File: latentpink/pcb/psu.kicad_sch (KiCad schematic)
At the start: 110 parts, among them J13 CONN_01X05, J14 CONN_01X03, J6 BARREL_JACK, U10 MYMGK1R812ERSR, U11 MYMGK00504ERSR, U12 STM32L031-QFN32, U13 MYMGK00504ERSR, U14 MYMGK00504ERSR, U15 MYMGK00504ERSR, U16 NCP45521IMNTWG-H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

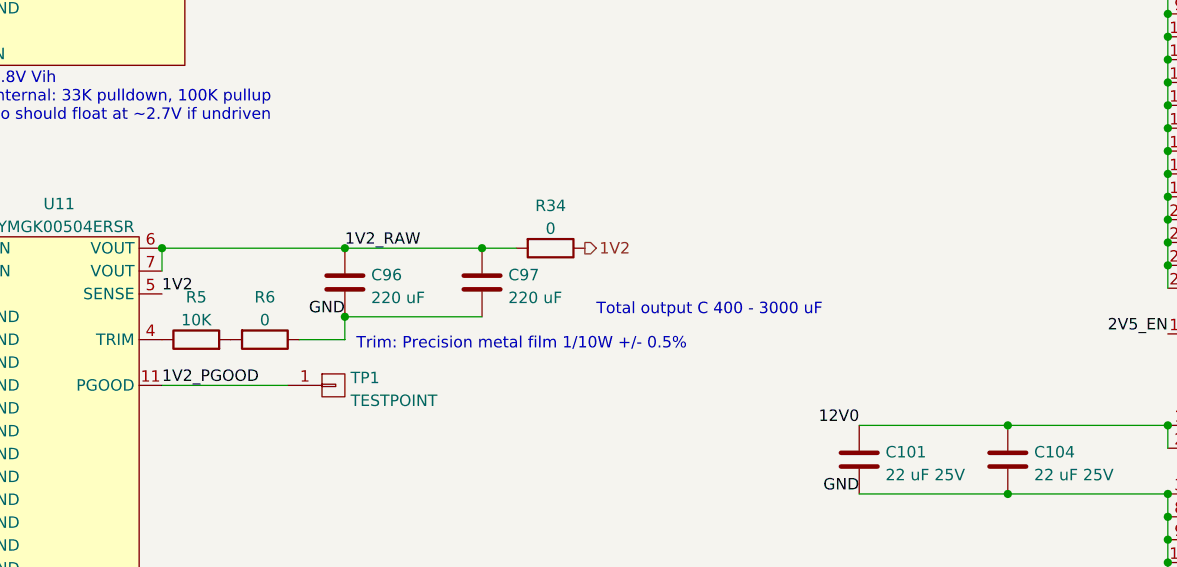
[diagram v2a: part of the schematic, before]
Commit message: Continued work on signoff review, added some more test points and SFP+ activity LEDs
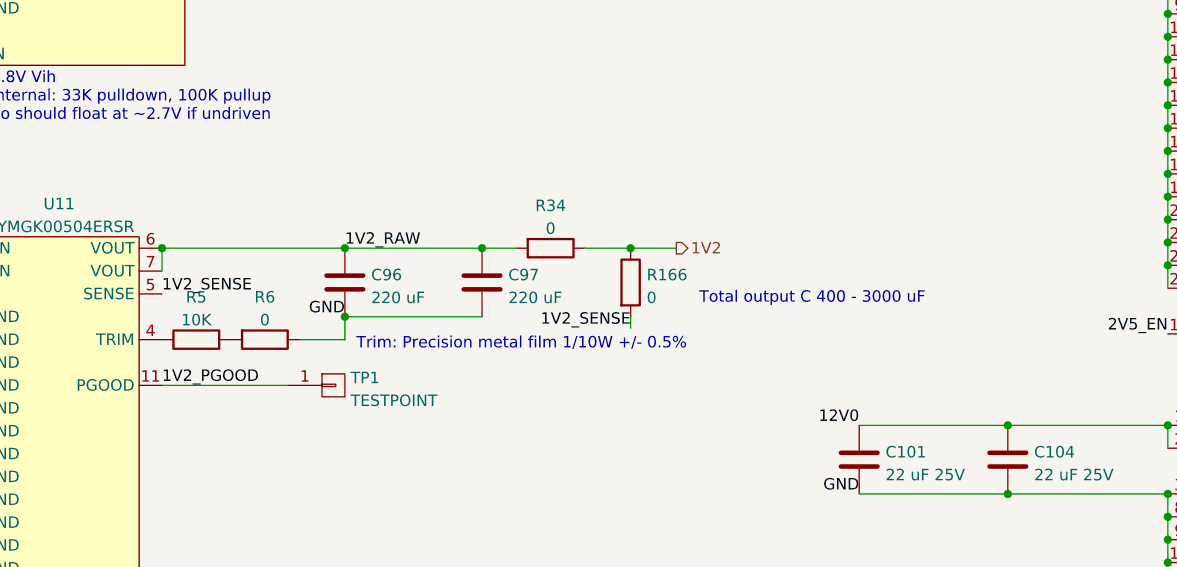
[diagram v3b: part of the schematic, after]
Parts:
- added R166: 0, azonenberg_pcb:EIA_0402_RES_NOSILK, symbol device:R
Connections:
- net 1V2: now also R166.1; no longer U11.5 (SENSE)
- new net 1V2_SENSE: R166.2, U11.5 (SENSE)
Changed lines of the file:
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@@
   (paper "A3")
   (title_block
-    (date "2023-05-20")
+    (date "2023-05-21")
     (rev "0.1")
     (company "Antikernel Labs")
@@
   (junction (at 260.35 102.235) (diameter 0) (color 0 0 0 0)
   )
+  (junction (at 129.54 140.97) (diameter 0) (color 0 0 0 0)
+  )
   (junction (at 374.65 246.38) (diameter 0) (color 0 0 0 0)
   )
@@
     (stroke (width 0) (type default) (color 0 0 0 0))
   )
+  (wire (pts (xy 129.54 148.59) (xy 129.54 149.86))
+    (stroke (width 0) (type default) (color 0 0 0 0))
+  )
   (wire (pts (xy 361.95 246.38) (xy 374.65 246.38))
     (stroke (width 0) (type default) (color 0 0 0 0))
@@
     (stroke (width 0) (type default) (color 0 0 0 0))
   )
+  (wire (pts (xy 129.54 140.97) (xy 134.62 140.97))
+    (stroke (width 0) (type default) (color 0 0 0 0))
+  )
   (wire (pts (xy 54.61 50.8) (xy 54.61 53.34))
     (stroke (width 0) (type default) (color 0 0 0 0))
@@
     (stroke (width 0) (type default) (color 0 0 0 0))
   )
+  (wire (pts (xy 124.46 140.97) (xy 129.54 140.97))
+    (stroke (width 0) (type default) (color 0 0 0 0))
+  )
   (wire (pts (xy 155.575 44.45) (xy 172.085 44.45))
     (stroke (width 0) (type default) (color 0 0 0 0))
@@
     (stroke (width 0) (type default) (color 0 0 0 0))
   )
-  (text "Total output C 400 - 3000 uF" (at 125.73 148.59 0)
+  (text "Total output C 400 - 3000 uF" (at 137.16 147.32 0)
     (effects (font (size 1.27 1.27)) (justify left bottom))
   )
@@
     (effects (font (size 1.27 1.27)) (justify right bottom))
   )
+  (label "1V2_SENSE" (at 129.54 149.86 180)
+    (effects (font (size 1.27 1.27)) (justify right bottom))
+  )
   (label "SUPER_RST_N" (at 255.27 261.62 180)
     (effects (font (size 1.27 1.27)) (justify right bottom))
@@
     (effects (font (size 1.27 1.27)) (justify right bottom))
   )
-  (label "1V2" (at 77.47 146.05 0)
+  (label "1V2_SENSE" (at 77.47 146.05 0)
     (effects (font (size 1.27 1.27)) (justify left bottom))
   )
@@
     (effects (font (size 1.27 1.27)) (justify left))
   )
-  (hierarchical_label "1V2" (shape output) (at 124.46 140.97 0)
+  (hierarchical_label "1V2" (shape output) (at 134.62 140.97 0)
     (effects (font (size 1.27 1.27)) (justify left))
   )
@@
       (effects (font (size 1.27 1.27)) hide)
     )
+    (pin "1")
+    (pin "2")
+  )
+  (symbol (lib_id "device:R") (at 129.54 144.78 0) (unit 1)
+    (in_bom yes) (on_board yes) (fields_autoplaced)
+    (property "Reference" "R166" (id 0) (at 131.318 143.9453 0)
+      (effects (font (size 1.27 1.27)) (justify left))
+    )
+    (property "Value" "0" (id 1) (at 131.318 146.4822 0)
+      (effects (font (size 1.27 1.27)) (justify left))
+    )
+    (property "Footprint" "azonenberg_pcb:EIA_0402_RES_NOSILK" (id 2) (at 127.762 144.78 90)
+      (effects (font (size 1.27 1.27)) hide)
+    )
+    (property "Datasheet" "" (id 3) (at 129.54 144.78 0)
+      (effects (font (size 1.27 1.27)) hide)
+    )

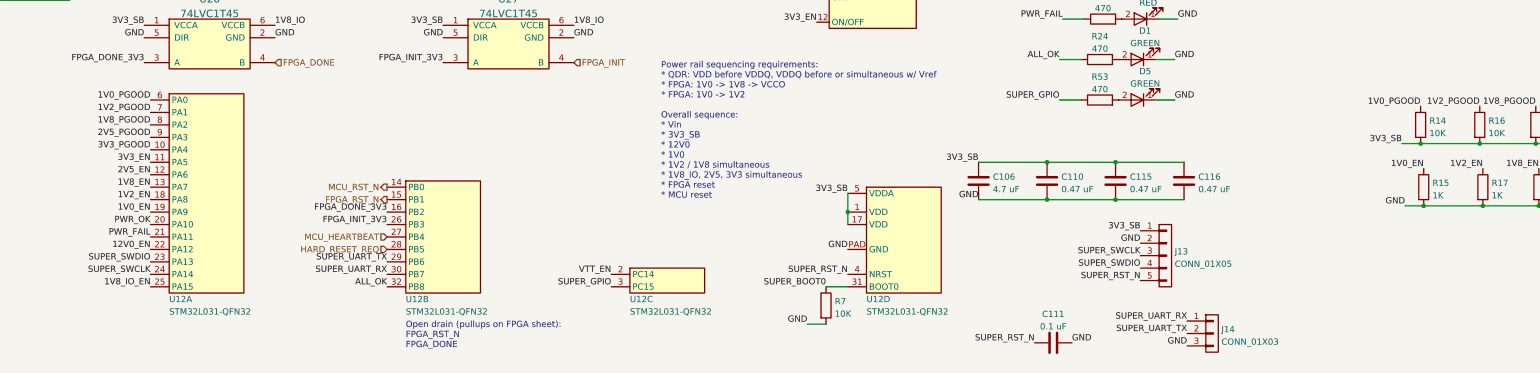
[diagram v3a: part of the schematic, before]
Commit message: Finished initial schematic review, added ESD diodes to Ethernet pairs
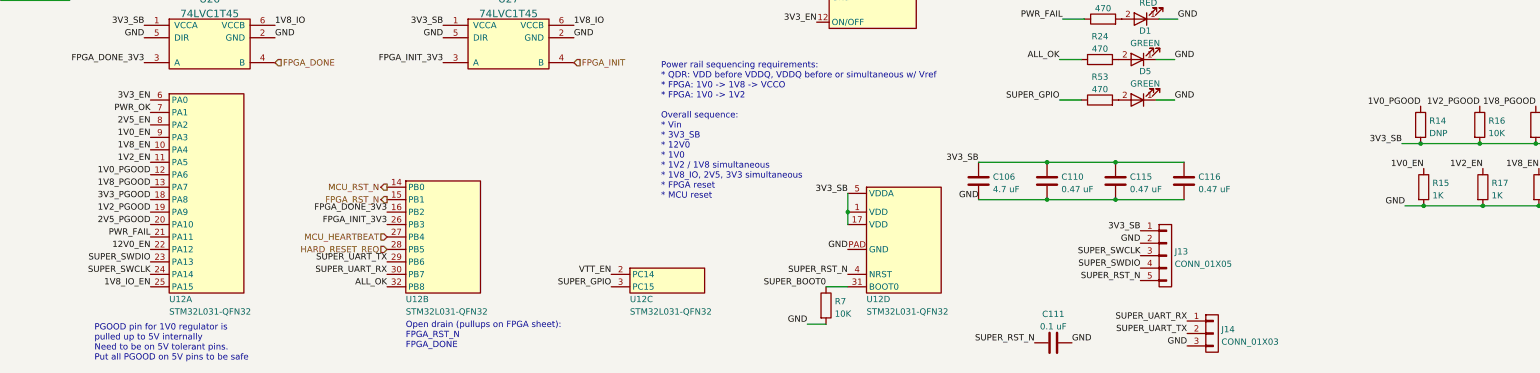
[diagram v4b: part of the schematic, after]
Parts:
- R14: value 10K -> DNP
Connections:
- net 1V0_EN: now also U12.9 (PA3); no longer U12.19 (PA9)
- net 1V0_PGOOD: now also U12.12 (PA6); no longer U12.6 (PA0)
- net 1V2_EN: now also U12.11 (PA5); no longer U12.18 (PA8)
- net 1V2_PGOOD: now also U12.19 (PA9); no longer U12.7 (PA1)
- net 1V8_EN: now also U12.10 (PA4); no longer U12.13 (PA7)
- net 1V8_PGOOD: now also U12.13 (PA7); no longer U12.8 (PA2)
- net 2V5_EN: now also U12.8 (PA2); no longer U12.12 (PA6)
- net 2V5_PGOOD: now also U12.20 (PA10); no longer U12.9 (PA3)
- net 3V3_EN: now also U12.6 (PA0); no longer U12.11 (PA5)
- net 3V3_PGOOD: now also U12.18 (PA8); no longer U12.10 (PA4)
- net PWR_OK: now also U12.7 (PA1); no longer U12.20 (PA10)
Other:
- note added: "PGOOD pin for 1V0 regulator is pulled up to 5V internally Need to be on 5V tolerant pins. Put all PGOOD on 5V pins to be safe"
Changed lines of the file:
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@@
+    (effects (font (size 1.27 1.27)) (justify left bottom))
+  )
+  (text "PGOOD pin for 1V0 regulator is\npulled up to 5V internally\nNeed to be on 5V tolerant pins.\nPut all PGOOD on 5V pins to be safe"
+    (at 41.91 278.13 0)
     (effects (font (size 1.27 1.27)) (justify left bottom))
   )
@@
     (effects (font (size 1.27 1.27)) (justify left bottom))
   )
-  (label "1V2_EN" (at 53.34 245.11 180)
+  (label "1V2_EN" (at 53.34 237.49 180)
     (effects (font (size 1.27 1.27)) (justify right bottom))
   )
@@
     (effects (font (size 1.27 1.27)) (justify left bottom))
   )
-  (label "3V3_PGOOD" (at 53.34 234.95 180)
+  (label "3V3_PGOOD" (at 53.34 245.11 180)
     (effects (font (size 1.27 1.27)) (justify right bottom))
   )
@@
     (effects (font (size 1.27 1.27)) (justify left bottom))
   )
-  (label "1V8_PGOOD" (at 53.34 229.87 180)
+  (label "1V8_PGOOD" (at 53.34 242.57 180)
     (effects (font (size 1.27 1.27)) (justify right bottom))
   )
@@
     (effects (font (size 1.27 1.27)) (justify right bottom))
   )
-  (label "2V5_PGOOD" (at 53.34 232.41 180)
+  (label "2V5_PGOOD" (at 53.34 250.19 180)
     (effects (font (size 1.27 1.27)) (justify right bottom))
   )
@@
     (effects (font (size 1.27 1.27)) (justify right bottom))
   )
-  (label "1V0_PGOOD" (at 53.34 224.79 180)
+  (label "1V0_PGOOD" (at 53.34 240.03 180)
     (effects (font (size 1.27 1.27)) (justify right bottom))
   )
@@
     (effects (font (size 1.27 1.27)) (justify left bottom))
   )
-  (label "1V0_EN" (at 53.34 247.65 180)
+  (label "1V0_EN" (at 53.34 232.41 180)
     (effects (font (size 1.27 1.27)) (justify right bottom))
   )
@@
     (effects (font (size 1.27 1.27)) (justify right bottom))
   )
-  (label "1V2_PGOOD" (at 53.34 227.33 180)
+  (label "1V2_PGOOD" (at 53.34 247.65 180)
     (effects (font (size 1.27 1.27)) (justify right bottom))
   )
@@
     (effects (font (size 1.27 1.27)) (justify right bottom))
   )
-  (label "PWR_OK" (at 53.34 250.19 180)
+  (label "PWR_OK" (at 53.34 227.33 180)
     (effects (font (size 1.27 1.27)) (justify right bottom))
   )
@@
     (effects (font (size 1.27 1.27)) (justify right bottom))
   )
-  (label "2V5_EN" (at 53.34 240.03 180)
+  (label "2V5_EN" (at 53.34 229.87 180)
     (effects (font (size 1.27 1.27)) (justify right bottom))
   )
@@
     (effects (font (size 1.27 1.27)) (justify right bottom))
   )
-  (label "1V8_EN" (at 53.34 242.57 180)
+  (label "1V8_EN" (at 53.34 234.95 180)
     (effects (font (size 1.27 1.27)) (justify right bottom))
   )
@@
     (effects (font (size 1.27 1.27)) (justify right bottom))
   )
-  (label "3V3_EN" (at 53.34 237.49 180)
+  (label "3V3_EN" (at 53.34 224.79 180)
     (effects (font (size 1.27 1.27)) (justify right bottom))
   )
@@
       (effects (font (size 1.27 1.27)) (justify left))
     )
-    (property "Value" "10K" (id 1) (at 314.198 231.5722 0)
-      (effects (font (size 1.27 1.27)) (justify left))
-    )
+    (property "Value" "DNP" (id 1) (at 314.198 231.5722 0)
+      (effects (font (size 1.27 1.27)) (justify left))
+    )

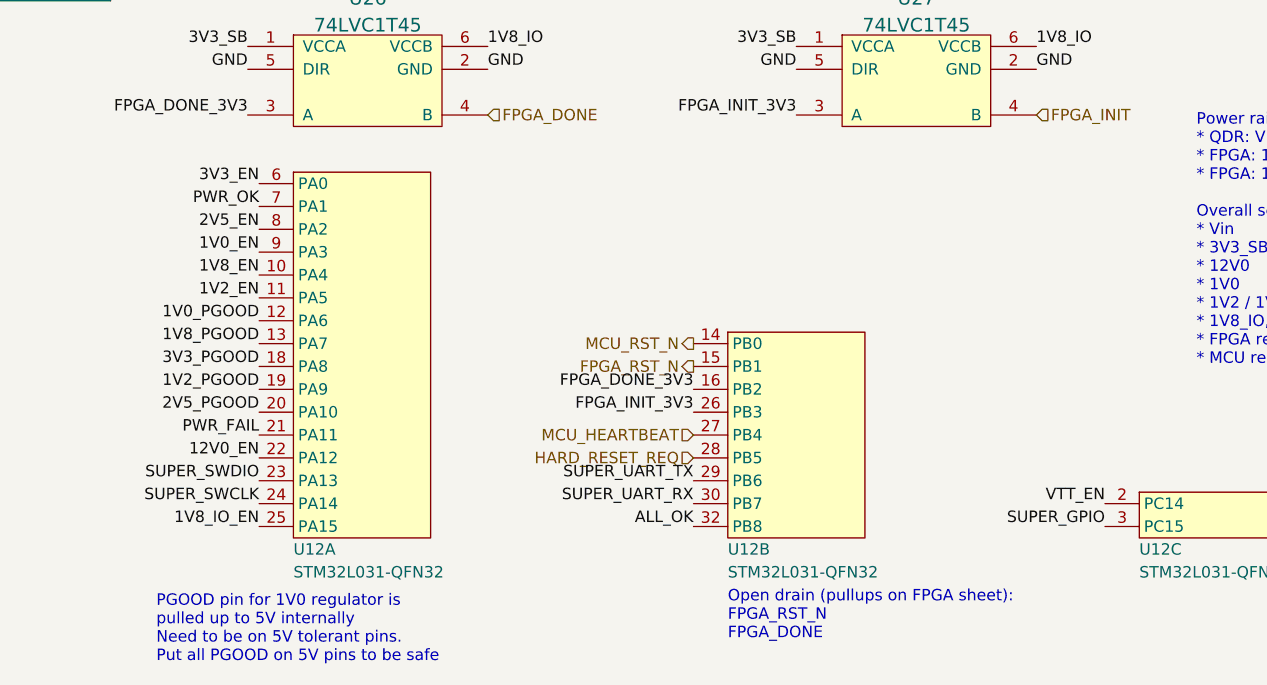
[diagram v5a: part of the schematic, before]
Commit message: Lots of layout progress on bottom power/management/supervisor area
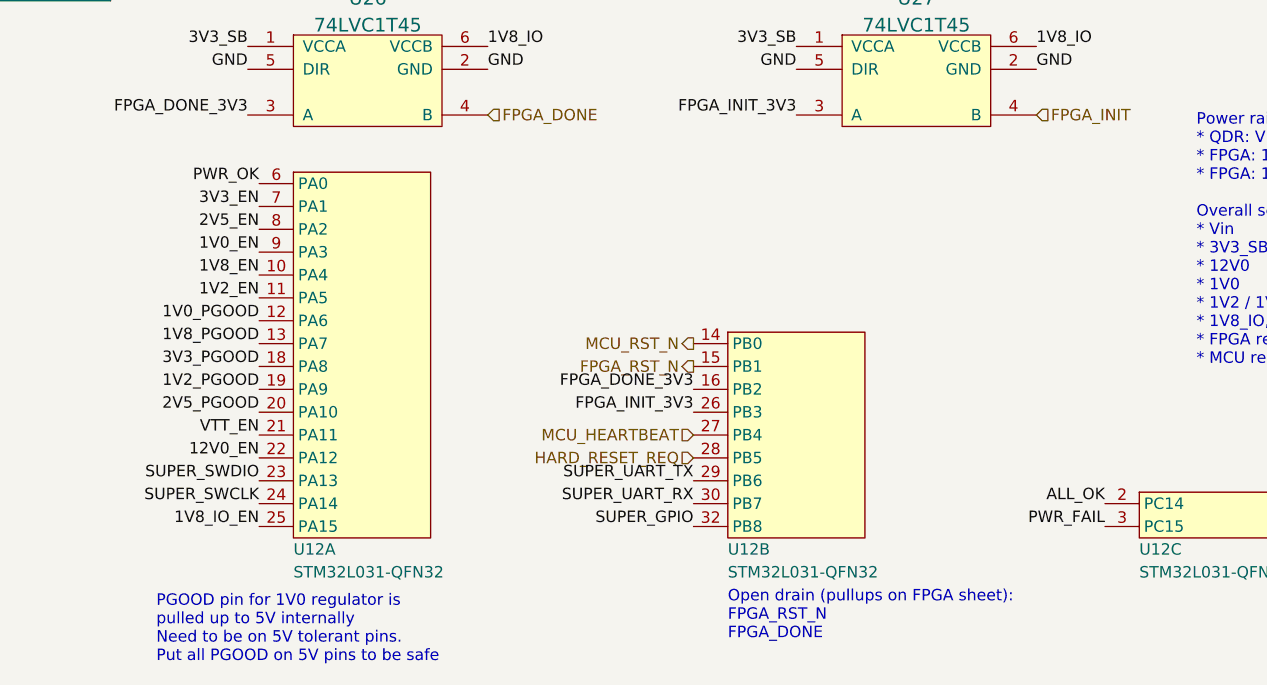
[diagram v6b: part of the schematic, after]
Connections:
- net 3V3_EN: now also U12.7 (PA1); no longer U12.6 (PA0)
- net ALL_OK: now also U12.2 (PC14); no longer U12.32 (PB8)
- net PWR_FAIL: now also U12.3 (PC15); no longer U12.21 (PA11)
- net PWR_OK: now also U12.6 (PA0); no longer U12.7 (PA1)
- net SUPER_GPIO: now also U12.32 (PB8); no longer U12.3 (PC15)
- net VTT_EN: now also U12.21 (PA11); no longer U12.2 (PC14)
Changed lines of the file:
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@@
   (paper "A3")
   (title_block
-    (date "2023-05-23")
+    (date "2023-05-27")
     (rev "0.1")
     (company "Antikernel Labs")
@@
     (effects (font (size 1.27 1.27)) (justify left bottom))
   )
-  (label "VTT_EN" (at 147.32 260.35 180)
+  (label "VTT_EN" (at 53.34 252.73 180)
     (effects (font (size 1.27 1.27)) (justify right bottom))
   )
@@
     (effects (font (size 1.27 1.27)) (justify right bottom))
   )
-  (label "ALL_OK" (at 101.6 262.89 180)
+  (label "ALL_OK" (at 147.32 260.35 180)
     (effects (font (size 1.27 1.27)) (justify right bottom))
   )
@@
     (effects (font (size 1.27 1.27)) (justify left bottom))
   )
-  (label "SUPER_GPIO" (at 147.32 262.89 180)
+  (label "SUPER_GPIO" (at 101.6 262.89 180)
     (effects (font (size 1.27 1.27)) (justify right bottom))
   )
@@
     (effects (font (size 1.27 1.27)) (justify right bottom))
   )
-  (label "PWR_OK" (at 53.34 227.33 180)
+  (label "PWR_OK" (at 53.34 224.79 180)
     (effects (font (size 1.27 1.27)) (justify right bottom))
   )
@@
     (effects (font (size 1.27 1.27)) (justify right bottom))
   )
-  (label "PWR_FAIL" (at 53.34 252.73 180)
-    (effects (font (size 1.27 1.27)) (justify right bottom))
-  )
-  (label "3V3_EN" (at 53.34 224.79 180)
-    (effects (font (size 1.27 1.27)) (justify right bottom))
-  )
+  (label "PWR_FAIL" (at 147.32 262.89 180)
+    (effects (font (size 1.27 1.27)) (justify right bottom))
+  )
+  (label "3V3_EN" (at 53.34 227.33 180)
+    (effects (font (size 1.27 1.27)) (justify right bottom))
+  )

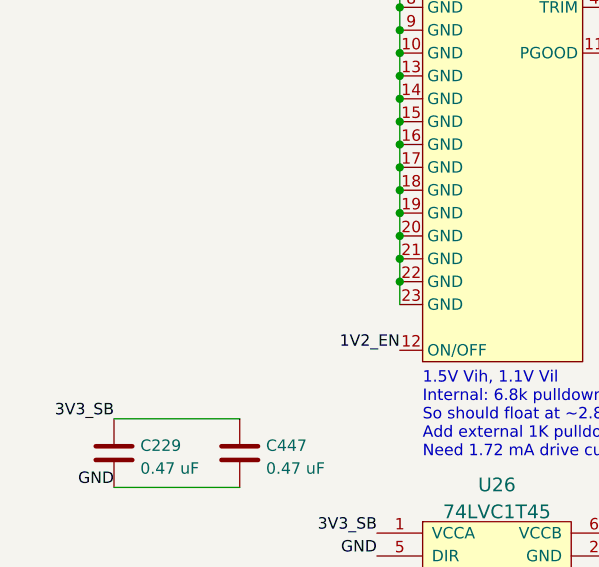
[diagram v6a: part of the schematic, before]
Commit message: Routed upper SGMII PHY except for bus to FPGA
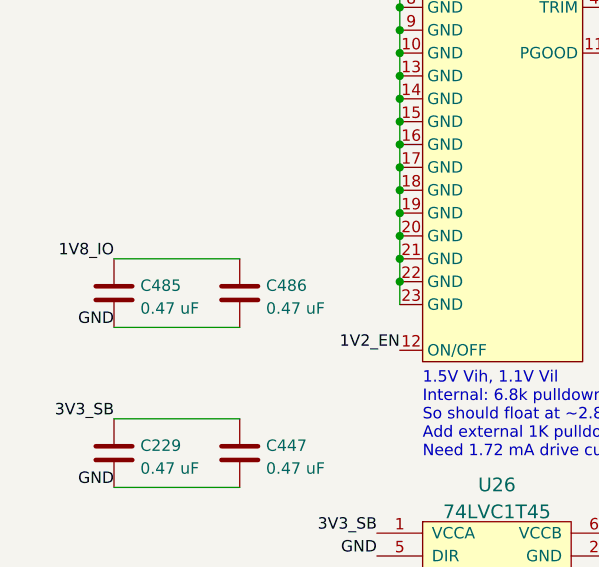
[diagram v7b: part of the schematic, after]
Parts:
- added C485, C486: 0.47 uF, azonenberg_pcb:EIA_0402_CAP_NOSILK, symbol device:C
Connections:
- net 1V8_IO: now also C485.1, C486.1
- net GND: now also C485.2, C486.2
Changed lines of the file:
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@@
   (paper "A3")
   (title_block
-    (date "2023-05-27")
+    (date "2023-05-28")
     (rev "0.1")
     (company "Antikernel Labs")
@@
     (stroke (width 0) (type default) (color 0 0 0 0))
   )
+  (wire (pts (xy 22.86 186.69) (xy 36.83 186.69))
+    (stroke (width 0) (type default) (color 0 0 0 0))
+  )
   (wire (pts (xy 259.08 190.5) (xy 262.89 190.5))
     (stroke (width 0) (type default) (color 0 0 0 0))
@@
   )
   (wire (pts (xy 170.18 24.13) (xy 184.15 24.13))
+    (stroke (width 0) (type default) (color 0 0 0 0))
+  )
+  (wire (pts (xy 22.86 179.07) (xy 36.83 179.07))
     (stroke (width 0) (type default) (color 0 0 0 0))
   )
@@
     (effects (font (size 1.27 1.27)) (justify right bottom))
   )
+  (label "GND" (at 22.86 186.69 180)
+    (effects (font (size 1.27 1.27)) (justify right bottom))
+  )
   (label "3V3" (at 327.66 167.64 180)
     (effects (font (size 1.27 1.27)) (justify right bottom))
@@
   (label "GND" (at 374.65 83.82 0)
     (effects (font (size 1.27 1.27)) (justify left bottom))
+  )
+  (label "1V8_IO" (at 22.86 179.07 180)
+    (effects (font (size 1.27 1.27)) (justify right bottom))
   )
   (label "GND" (at 78.74 212.09 0)
@@
     )
     (property "Datasheet" "" (id 3) (at 173.99 35.56 0)
+      (effects (font (size 1.27 1.27)) hide)
+    )
+    (pin "1")
+    (pin "2")
+  )
+  (symbol (lib_id "device:C") (at 22.86 182.88 0) (unit 1)
+    (in_bom yes) (on_board yes) (fields_autoplaced)
+    (property "Reference" "C485" (id 0) (at 25.781 182.0453 0)
+      (effects (font (size 1.27 1.27)) (justify left))
+    )
+    (property "Value" "0.47 uF" (id 1) (at 25.781 184.5822 0)
+      (effects (font (size 1.27 1.27)) (justify left))
+    )
+    (property "Footprint" "azonenberg_pcb:EIA_0402_CAP_NOSILK" (id 2) (at 23.8252 186.69 0)
+      (effects (font (size 1.27 1.27)) hide)
+    )
+    (property "Datasheet" "" (id 3) (at 22.86 182.88 0)
       (effects (font (size 1.27 1.27)) hide)
     )
@@
       (effects (font (size 1.27 1.27)) hide)
     )
+    (pin "1")
+    (pin "2")
+  )
+  (symbol (lib_id "device:C") (at 36.83 182.88 0) (unit 1)
+    (in_bom yes) (on_board yes) (fields_autoplaced)
+    (property "Reference" "C486" (id 0) (at 39.751 182.0453 0)
+      (effects (font (size 1.27 1.27)) (justify left))
+    )
+    (property "Value" "0.47 uF" (id 1) (at 39.751 184.5822 0)
+      (effects (font (size 1.27 1.27)) (justify left))
+    )
+    (property "Footprint" "azonenberg_pcb:EIA_0402_CAP_NOSILK" (id 2) (at 37.7952 186.69 0)
+      (effects (font (size 1.27 1.27)) hide)
+    )
+    (property "Datasheet" "" (id 3) (at 36.83 182.88 0)
+      (effects (font (size 1.27 1.27)) hide)
+    )
